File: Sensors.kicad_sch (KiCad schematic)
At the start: 175 parts, among them U1 SW_MX_HE, U10 SW_MX_HE, U11 SW_MX_HE, U12 SW_MX_HE, U13 SW_MX_HE, U14 SW_MX_HE, U15 SW_MX_HE, U16 SW_MX_HE, U17 SW_MX_HE, U18 SW_MX_HE, U19 SW_MX_HE, U2 SW_MX_HE, U20 SW_MX_HE, U21 SW_MX_HE, U22 SW_MX_HE, U23 SW_MX_HE, U24 SW_MX_HE, U25 SW_MX_HE, U26 SW_MX_HE, U27 SW_MX_HE, U28 SW_MX_HE, U29 SW_MX_HE, U3 SW_MX_HE, U30 SW_MX_HE, U31 SW_MX_HE, U32 SW_MX_HE, U33 SW_MX_HE, U34 SW_MX_HE, U35 SW_MX_HE, U36 SW_MX_HE, U37 SW_MX_HE, U38 SW_MX_HE, U39 SW_MX_HE, U4 SW_MX_HE, U40 SW_MX_HE, U41 SW_MX_HE, U42 SW_MX_HE, U43 SW_MX_HE, U44 SW_MX_HE, U45 SW_MX_HE, U46 SW_MX_HE, U47 SW_MX_HE, U48 SW_MX_HE, U49 SW_MX_HE, U5 SW_MX_HE, U50 SW_MX_HE, U51 SW_MX_HE, U52 SW_MX_HE, U53 SW_MX_HE, U54 SW_MX_HE, U55 SW_MX_HE, U56 SW_MX_HE, U57 SW_MX_HE, U58 SW_MX_HE, U59 SW_MX_HE, U6 SW_MX_HE, U60 SW_MX_HE, U61 SW_MX_HE, U62 SW_MX_HE, U63 SW_MX_HE, U64 SW_MX_HE, U65 SW_MX_HE, U66 SW_MX_HE, U67 SW_MX_HE, U68 SW_MX_HE, U69 SW_MX_HE, U7 SW_MX_HE, U70 SW_MX_HE, U71 SW_MX_HE, U72 SW_MX_HE, U73 SW_MX_HE, U74 SW_MX_HE, U75 SW_MX_HE, U8 SW_MX_HE, U9 SW_MX_HE

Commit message: initial commit
i made the board yay!
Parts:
- S1, S2, S3, S4, S5: now left out of the parts list
- U62, U63, U64, U75: footprint PCM_marbastlib-he:SW_MX_HE_90deg_1u -> PCM_marbastlib-he:SW_MX_HE_90deg_NoVia
- renumbered AM401 to AM501, AM402 to AM502, AM403 to AM503, AM404 to AM504, AM405 to AM505, AM406 to AM506, AM407 to AM507, AM408 to AM508, AM409 to AM509, AM410 to AM510, C401 to C501, C402 to C502, C403 to C503, C404 to C504, C405 to C505, C406 to C506, C407 to C507, C408 to C508, C409 to C509, C410 to C510
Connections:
- net GND: now also AM504.2 (X6), AM505.14 (X1), AM506.2 (X6), AM507.2 (X6), AM507.5 (X5)
- net HE1: now also AM509.13 (X0)
- net HE10: now also AM505.15 (X2)
- net HE11: now also AM506.12 (X3)
- net HE12: now also AM506.13 (X0)
- net HE13: now also AM507.12 (X3)
- net HE14: now also AM508.12 (X3)
- net HE15: now also AM509.12 (X3)
- net HE16: now also AM509.14 (X1)
- net HE17: now also AM510.12 (X3)
- net HE18: now also AM501.5 (X5)
- net HE19: now also AM502.5 (X5)
- net HE2: now also AM509.15 (X2)
- net HE20: now also AM502.15 (X2)
- net HE21: now also AM503.4 (X7)
- net HE22: now also AM504.5 (X5)
- net HE23: now also AM504.13 (X0)
- net HE24: now also AM505.4 (X7)
- net HE25: now also AM506.5 (X5)
- net HE26: now also AM506.15 (X2)
- net HE27: now also AM507.4 (X7)
- net HE28: now also AM508.5 (X5)
- net HE29: now also AM508.14 (X1)
- net HE3: now also AM501.12 (X3)
- net HE30: now also AM509.4 (X7)
- net HE31: now also AM510.5 (X5)
- net HE32: now also AM510.14 (X1)
- net HE33: now also AM501.4 (X7)
- net HE34: now also AM501.2 (X6)
- net HE35: now also AM502.4 (X7)
- net HE36: now also AM503.5 (X5)
- net HE37: now also AM503.13 (X0)
- net HE38: now also AM504.4 (X7)
- net HE39: now also AM504.14 (X1)
- net HE4: now also AM501.15 (X2)
- net HE40: now also AM505.2 (X6)
- net HE41: now also AM506.4 (X7)
- net HE42: now also AM506.14 (X1)
- net HE43: now also AM507.13 (X0)
- net HE44: now also AM508.4 (X7)
- net HE45: now also AM508.15 (X2)
- net HE46: now also AM509.1 (X4)
- net HE47: now also AM510.15 (X2)
- net HE48: now also AM501.14 (X1)
- net HE49: now also AM502.13 (X0)
- net HE5: now also AM502.12 (X3)
- net HE50: now also AM503.1 (X4)
- net HE51: now also AM503.14 (X1)
- net HE52: now also AM504.1 (X4)
- net HE53: now also AM504.15 (X2)
- net HE54: now also AM505.13 (X0)
- net HE55: now also AM506.1 (X4)
- net HE56: now also AM507.1 (X4)
- net HE57: now also AM507.14 (X1)
- net HE58: now also AM508.2 (X6)
- net HE59: now also AM509.5 (X5)
- net HE6: now also AM503.12 (X3)
- net HE60: now also AM510.4 (X7)
- net HE61: now also AM510.13 (X0)
- net HE62: now also AM501.1 (X4)
- net HE63: now also AM502.2 (X6)
- net HE64: now also AM502.14 (X1)
- net HE65: now also AM505.5 (X5)
- net HE66: now also AM507.15 (X2)
- net HE67: now also AM508.13 (X0)
- net HE68: now also AM509.2 (X6)
- net HE69: now also AM510.2 (X6)
- net HE7: now also AM503.15 (X2)
- net HE70: now also AM510.1 (X4)
- net HE71: now also AM501.13 (X0)
- net HE72: now also AM502.1 (X4)
- net HE73: now also AM503.2 (X6)
- net HE74: now also AM505.1 (X4)
- net HE75: now also AM508.1 (X4)
- net HE8: now also AM504.12 (X3)
- net HE9: now also AM505.12 (X3)
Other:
- note added: "x"
- note removed: "4xx"

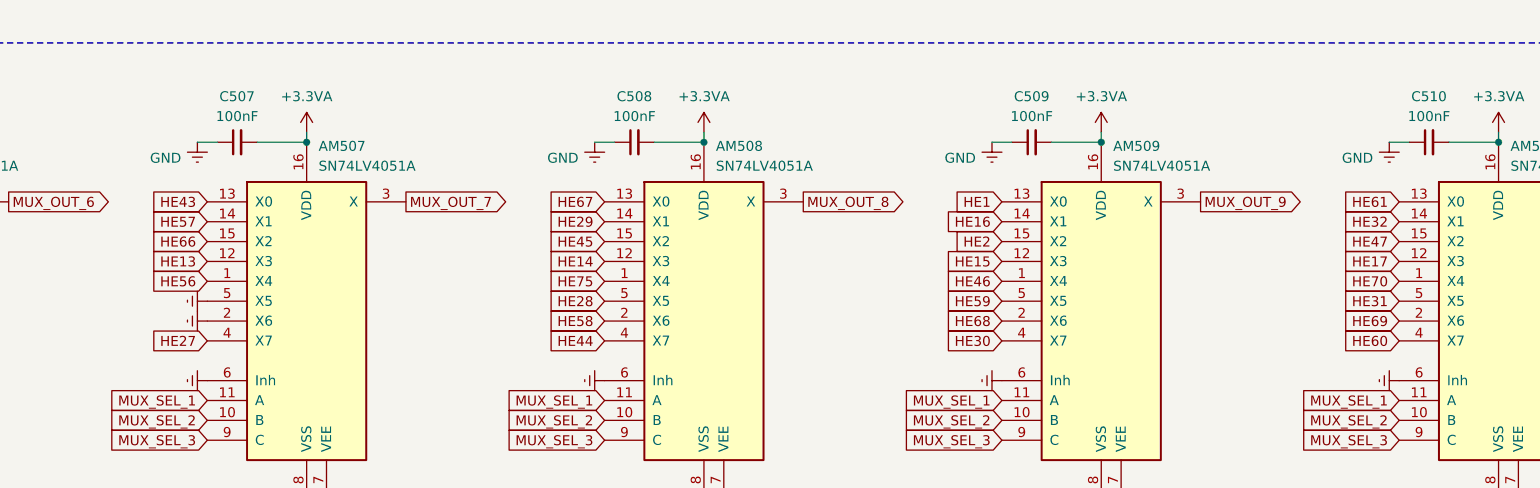
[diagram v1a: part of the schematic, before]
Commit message: no rounded tracks
routed the pcb again but without rounding the tracks because kicad became laggy af
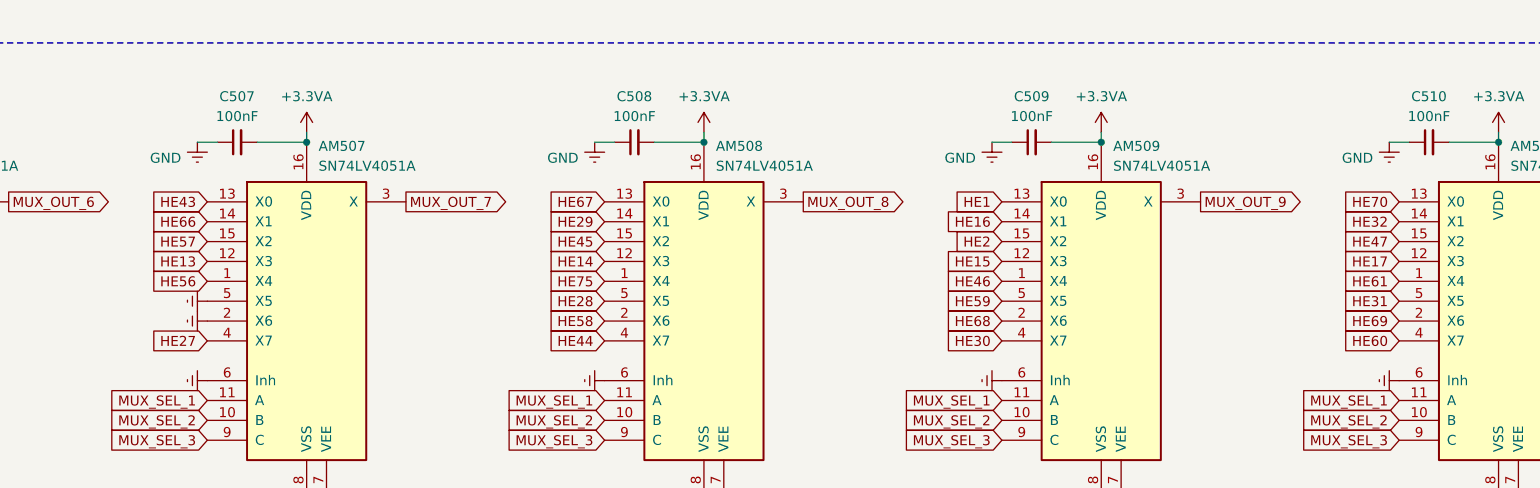
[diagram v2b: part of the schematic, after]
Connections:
- net HE57: now also AM507.15 (X2); no longer AM507.14 (X1)
- net HE61: now also AM510.1 (X4); no longer AM510.13 (X0)
- net HE66: now also AM507.14 (X1); no longer AM507.15 (X2)
- net HE70: now also AM510.13 (X0); no longer AM510.1 (X4)

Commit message: full PCB and BOM
the pcb is done (i hope) and i made the production files and filled out the bom with parts from lcsc
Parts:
- renumbered C3 to C1, C12 to C10, C13 to C11, C14 to C12, C15 to C13, C1 to C14, C16 to C15, C2 to C16, C4 to C2, C5 to C3, C6 to C4, C7 to C5, C8 to C6, C71 to C63, C63 to C64, C72 to C65, C64 to C66, C73 to C67, C65 to C68, C74 to C69, C9 to C7, C66 to C70, C75 to C71, C67 to C72, C68 to C73, C69 to C74, C70 to C75, C10 to C8, C11 to C9, U3 to U1, U12 to U10, U13 to U11, U14 to U12, U15 to U13, U1 to U14, U16 to U15, U2 to U16, U4 to U2, U5 to U3, U6 to U4, U7 to U5, U8 to U6, U71 to U63, U63 to U64, U72 to U65, U64 to U66, U73 to U67, U65 to U68, U74 to U69, U9 to U7, U66 to U70, U75 to U71, U67 to U72, U68 to U73, U69 to U74, U70 to U75, U10 to U8, U11 to U9
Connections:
- net HE1: now also AM501.12 (X3), U1.2 (VOUT); no longer AM509.13 (X0), U14.2 (VOUT)
- net HE10: now also AM506.13 (X0), U10.2 (VOUT); no longer AM505.15 (X2), U8.2 (VOUT)
- net HE11: now also AM507.12 (X3), U11.2 (VOUT); no longer AM506.12 (X3), U9.2 (VOUT)
- net HE12: now also AM508.12 (X3), U12.2 (VOUT); no longer AM506.13 (X0), U10.2 (VOUT)
- net HE13: now also AM509.12 (X3), U13.2 (VOUT); no longer AM507.12 (X3), U11.2 (VOUT)
- net HE14: now also AM509.13 (X0), U14.2 (VOUT); no longer AM508.12 (X3), U12.2 (VOUT)
- net HE15: now also AM509.14 (X1), U15.2 (VOUT); no longer AM509.12 (X3), U13.2 (VOUT)
- net HE16: now also AM509.15 (X2), U16.2 (VOUT); no longer AM509.14 (X1), U15.2 (VOUT)
- net HE2: now also AM501.15 (X2), U2.2 (VOUT); no longer AM509.15 (X2), U16.2 (VOUT)
- net HE3: now also AM502.12 (X3), U3.2 (VOUT); no longer AM501.12 (X3), U1.2 (VOUT)
- net HE4: now also AM503.12 (X3), U4.2 (VOUT); no longer AM501.15 (X2), U2.2 (VOUT)
- net HE5: now also AM503.15 (X2), U5.2 (VOUT); no longer AM502.12 (X3), U3.2 (VOUT)
- net HE6: now also AM504.12 (X3), U6.2 (VOUT); no longer AM503.12 (X3), U4.2 (VOUT)
- net HE63: now also AM501.13 (X0), U63.2 (VOUT); no longer AM502.2 (X6), U64.2 (VOUT)
- net HE64: now also AM502.2 (X6), U64.2 (VOUT); no longer AM502.14 (X1), U66.2 (VOUT)
- net HE65: now also AM502.1 (X4), U65.2 (VOUT); no longer AM505.5 (X5), U68.2 (VOUT)
- net HE66: now also AM502.14 (X1), U66.2 (VOUT); no longer AM507.14 (X1), U70.2 (VOUT)
- net HE67: now also AM503.2 (X6), U67.2 (VOUT); no longer AM508.13 (X0), U72.2 (VOUT)
- net HE68: now also AM505.5 (X5), U68.2 (VOUT); no longer AM509.2 (X6), U73.2 (VOUT)
- net HE69: now also AM505.1 (X4), U69.2 (VOUT); no longer AM510.2 (X6), U74.2 (VOUT)
- net HE7: now also AM505.12 (X3), U7.2 (VOUT); no longer AM503.15 (X2), U5.2 (VOUT)
- net HE70: now also AM507.14 (X1), U70.2 (VOUT); no longer AM510.13 (X0), U75.2 (VOUT)
- net HE71: now also AM508.1 (X4), U71.2 (VOUT); no longer AM501.13 (X0), U63.2 (VOUT)
- net HE72: now also AM508.13 (X0), U72.2 (VOUT); no longer AM502.1 (X4), U65.2 (VOUT)
- net HE73: now also AM509.2 (X6), U73.2 (VOUT); no longer AM503.2 (X6), U67.2 (VOUT)
- net HE74: now also AM510.2 (X6), U74.2 (VOUT); no longer AM505.1 (X4), U69.2 (VOUT)
- net HE75: now also AM510.13 (X0), U75.2 (VOUT); no longer AM508.1 (X4), U71.2 (VOUT)
- net HE8: now also AM505.15 (X2), U8.2 (VOUT); no longer AM504.12 (X3), U6.2 (VOUT)
- net HE9: now also AM506.12 (X3), U9.2 (VOUT); no longer AM505.12 (X3), U7.2 (VOUT)

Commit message: 1 less multiplexer!
made the whole board again to use only 1 sensor for each 1/8 unit pair of switches on the bottom row. i also made some improvements in the whole design itself
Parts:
- removed AM510: SN74LV4051A, Package_SO:TSSOP-16_4.4x5mm_P0.65mm, symbol 4xxx:4051
- removed C510, C63, C65, C67, C71: 100nF, Capacitor_SMD:C_0805_2012Metric, symbol Device:C_Small
- removed U63, U65, U67: SW_MX_HE, PCM_marbastlib-he:SW_MX_HE_90deg_1u, symbol PCM_marbastlib-he:SW_MX_HE
- removed U71: SW_MX_HE, PCM_marbastlib-he:SW_MX_HE_90deg_NoVia, symbol PCM_marbastlib-he:SW_MX_HE
- U33: footprint PCM_marbastlib-he:SW_MX_HE_90deg_1u -> PCM_marbastlib-he:SW_MX_HE_90deg_1.75u_STP_1.25
- U62: footprint PCM_marbastlib-he:SW_MX_HE_90deg_NoVia -> PCM_marbastlib-he:SW_MX_HE_90deg_1_8u
- U63: renamed from U64; footprint PCM_marbastlib-he:SW_MX_HE_90deg_NoVia -> PCM_marbastlib-he:SW_MX_HE_90deg_1_8u
- U64: renamed from U66; footprint PCM_marbastlib-he:SW_MX_HE_90deg_NoVia -> PCM_marbastlib-he:SW_MX_HE_90deg_1_8u
- U68: renamed from U72; footprint PCM_marbastlib-he:SW_MX_HE_90deg_1u -> PCM_marbastlib-he:SW_MX_HE_90deg_1_8u
- renumbered C64 to C63, C66 to C64, C68 to C65, C69 to C66, C70 to C67, C72 to C68, C73 to C69, C74 to C70, C75 to C71, U68 to U65, U69 to U66, U70 to U67, U73 to U69, U74 to U70, U75 to U71
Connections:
- net HE74 is gone; now on net HE70: U70.2 (VOUT)
- net HE75 is gone; now on net HE71: U71.2 (VOUT)
- net GND: now also AM505.12 (X3); no longer AM504.2 (X6), AM505.14 (X1), AM506.2 (X6), AM507.2 (X6), AM507.5 (X5)
- net HE1: now also AM501.4 (X7); no longer AM501.12 (X3)
- net HE10: now also AM506.4 (X7); no longer AM506.13 (X0)
- net HE11: now also AM507.1 (X4); no longer AM507.12 (X3)
- net HE12: now also AM507.2 (X6); no longer AM508.12 (X3)
- net HE13: now also AM508.1 (X4); no longer AM509.12 (X3)
- net HE14: now also AM508.2 (X6); no longer AM509.13 (X0)
- net HE15: now also AM508.4 (X7); no longer AM509.14 (X1)
- net HE16: now also AM508.5 (X5); no longer AM509.15 (X2)
- net HE17: now also AM509.4 (X7)
- net HE18: now also AM501.1 (X4); no longer AM501.5 (X5)
- net HE19: now also AM501.12 (X3); no longer AM502.5 (X5)
- net HE2: now also AM502.2 (X6); no longer AM501.15 (X2)
- net HE20: now also AM502.1 (X4); no longer AM502.15 (X2)
- net HE22: now also AM503.14 (X1); no longer AM504.5 (X5)
- net HE23: now also AM504.1 (X4); no longer AM504.13 (X0)
- net HE24: now also AM505.1 (X4); no longer AM505.4 (X7)
- net HE25: now also AM505.15 (X2); no longer AM506.5 (X5)
- net HE26: now also AM506.1 (X4); no longer AM506.15 (X2)
- net HE27: now also AM506.5 (X5); no longer AM507.4 (X7)
- net HE28: now also AM507.15 (X2); no longer AM508.5 (X5)
- net HE29: now also AM507.5 (X5); no longer AM508.14 (X1)
- net HE3: now also AM502.4 (X7); no longer AM502.12 (X3)
- net HE30: now also AM508.13 (X0); no longer AM509.4 (X7)
- net HE31: now also AM509.1 (X4)
- net HE32: now also AM509.5 (X5)
- net HE33: now also AM501.2 (X6); no longer AM501.4 (X7)
- net HE34: now also AM501.13 (X0); no longer AM501.2 (X6)
- net HE35: now also AM501.5 (X5); no longer AM502.4 (X7)
- net HE36: now also AM502.13 (X0); no longer AM503.5 (X5)
- net HE37: now also AM503.2 (X6); no longer AM503.13 (X0)
- net HE38: now also AM503.13 (X0); no longer AM504.4 (X7)
- net HE39: now also AM504.2 (X6); no longer AM504.14 (X1)
- net HE4: now also AM502.5 (X5); no longer AM503.12 (X3)
- net HE40: now also AM504.12 (X3); no longer AM505.2 (X6)
- net HE41: now also AM505.14 (X1); no longer AM506.4 (X7)
- net HE42: now also AM506.2 (X6); no longer AM506.14 (X1)
- net HE43: now also AM506.12 (X3); no longer AM507.13 (X0)
- net HE44: now also AM507.14 (X1); no longer AM508.4 (X7)
- net HE45: now also AM507.4 (X7); no longer AM508.15 (X2)
- net HE46: now also AM508.12 (X3); no longer AM509.1 (X4)
- net HE47: now also AM509.12 (X3)
- net HE48: now also AM501.15 (X2); no longer AM501.14 (X1)
- net HE49: now also AM502.14 (X1); no longer AM502.13 (X0)
- net HE5: now also AM503.5 (X5); no longer AM503.15 (X2)
- net HE51: now also AM503.15 (X2); no longer AM503.14 (X1)
- net HE52: now also AM503.12 (X3); no longer AM504.1 (X4)
- net HE54: now also AM505.2 (X6); no longer AM505.13 (X0)
- net HE55: now also AM505.13 (X0); no longer AM506.1 (X4)
- net HE56: now also AM506.15 (X2); no longer AM507.1 (X4)
- net HE57: now also AM506.13 (X0); no longer AM507.15 (X2)
- net HE58: now also AM507.13 (X0); no longer AM508.2 (X6)
- net HE59: now also AM508.15 (X2); no longer AM509.5 (X5)
- net HE6: now also AM504.4 (X7); no longer AM504.12 (X3)
- net HE60: now also AM509.2 (X6)
- net HE61: now also AM509.14 (X1)
- net HE62: now also AM501.14 (X1); no longer AM501.1 (X4)
- net HE63: now also AM502.15 (X2), U63.2 (VOUT); no longer AM501.13 (X0)
- net HE64: now also AM502.12 (X3), U64.2 (VOUT); no longer AM502.2 (X6), U63.2 (VOUT)
- net HE65: now also AM504.14 (X1), U65.2 (VOUT); no longer AM502.1 (X4)
- net HE66: now also AM504.13 (X0), U66.2 (VOUT); no longer AM502.14 (X1), U64.2 (VOUT)
- net HE67: now also AM506.14 (X1), U67.2 (VOUT); no longer AM503.2 (X6)
- net HE68: now also AM507.12 (X3), U68.2 (VOUT); no longer AM505.5 (X5), U65.2 (VOUT)
- net HE69: now also AM508.14 (X1), U69.2 (VOUT); no longer AM505.1 (X4), U66.2 (VOUT)
- net HE7: now also AM504.5 (X5); no longer AM505.12 (X3)
- net HE70: now also AM509.15 (X2); no longer AM507.14 (X1), U67.2 (VOUT)
- net HE71: now also AM509.13 (X0); no longer AM508.1 (X4)
- net HE8: now also AM505.4 (X7); no longer AM505.15 (X2)
- net HE9: now also AM505.5 (X5); no longer AM506.12 (X3)
- removed net HE72: AM508.13 (X0), U68.2 (VOUT)
- removed net HE73: AM509.2 (X6), U69.2 (VOUT)

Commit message: added test points
added test points to the pcb power lines and multiplexer outputs, hopefully the readme is fixed as well
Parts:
- added TP501: AM1, TestPoint:TestPoint_Pad_D2.0mm, symbol Connector:TestPoint
- added TP502: AM2, TestPoint:TestPoint_Pad_D2.0mm, symbol Connector:TestPoint
- added TP503: AM3, TestPoint:TestPoint_Pad_D2.0mm, symbol Connector:TestPoint
- added TP504: AM4, TestPoint:TestPoint_Pad_D2.0mm, symbol Connector:TestPoint
- added TP505: AM5, TestPoint:TestPoint_Pad_D2.0mm, symbol Connector:TestPoint
- added TP506: AM6, TestPoint:TestPoint_Pad_D2.0mm, symbol Connector:TestPoint
- added TP507: AM7, TestPoint:TestPoint_Pad_D2.0mm, symbol Connector:TestPoint
- added TP508: AM8, TestPoint:TestPoint_Pad_D2.0mm, symbol Connector:TestPoint
- added TP509: AM9, TestPoint:TestPoint_Pad_D2.0mm, symbol Connector:TestPoint
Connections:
- net MUX_OUT_1: now also TP501.1
- net MUX_OUT_2: now also TP502.1
- net MUX_OUT_3: now also TP503.1
- net MUX_OUT_4: now also TP504.1
- net MUX_OUT_5: now also TP505.1
- net MUX_OUT_6: now also TP506.1
- net MUX_OUT_7: now also TP507.1
- net MUX_OUT_8: now also TP508.1
- net MUX_OUT_9: now also TP509.1
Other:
- company: (none) -> Zohar Galili
- title: (none) -> sensors and multiplexers
